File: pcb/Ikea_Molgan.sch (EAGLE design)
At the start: 21 parts, among them U2 MEGA328P-AU

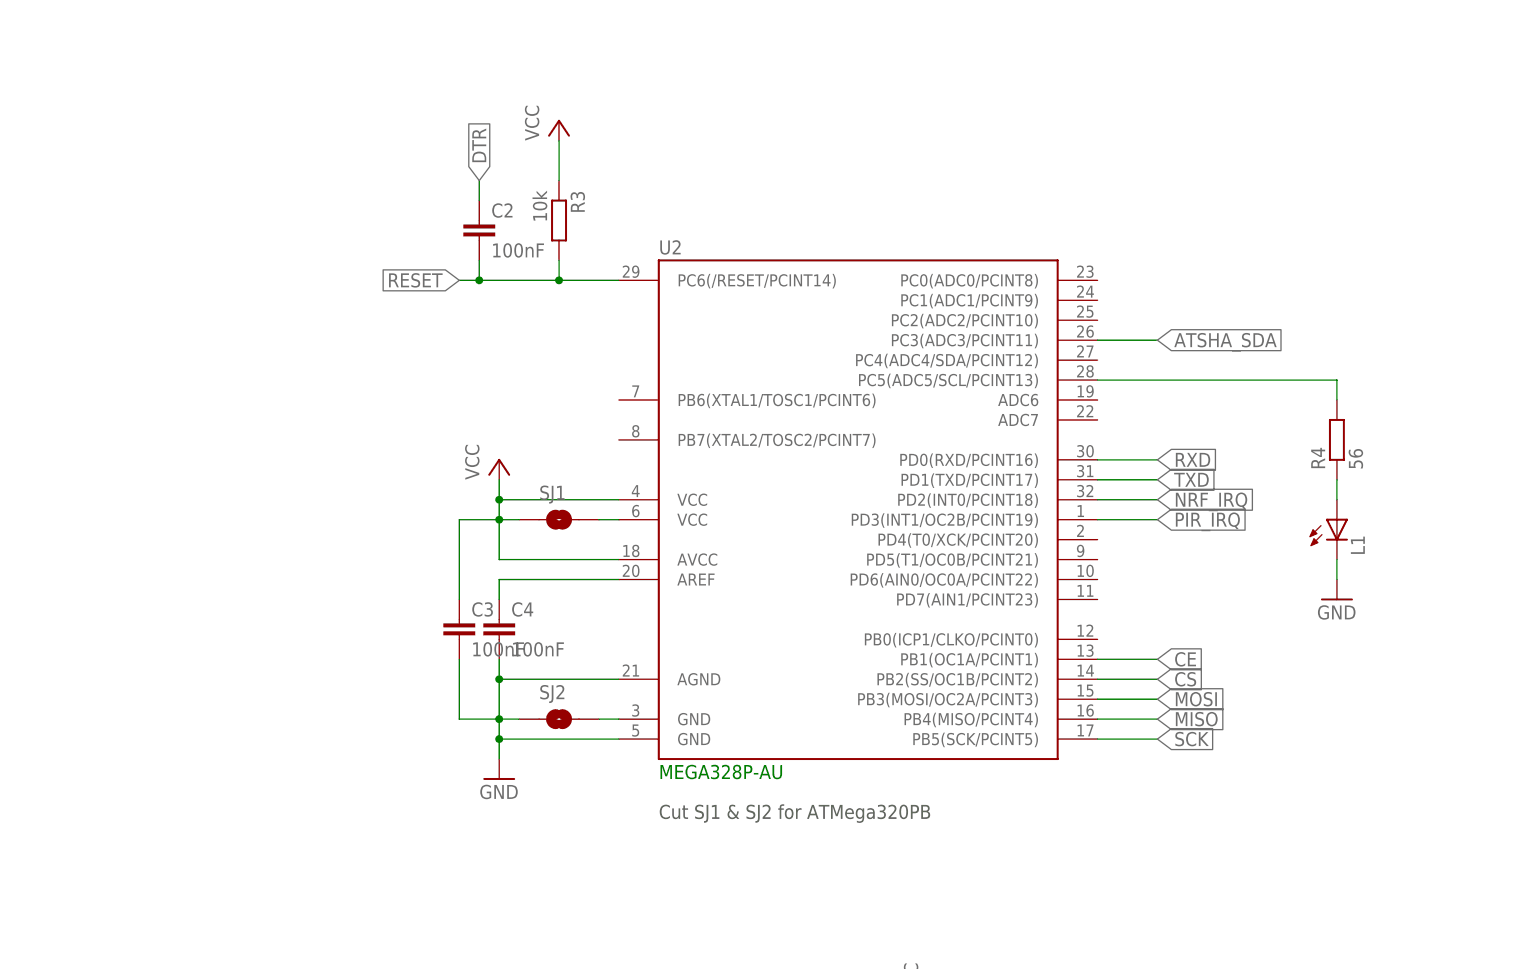
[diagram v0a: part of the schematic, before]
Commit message: Temperatursensor hinzugefügt und LED entfernt
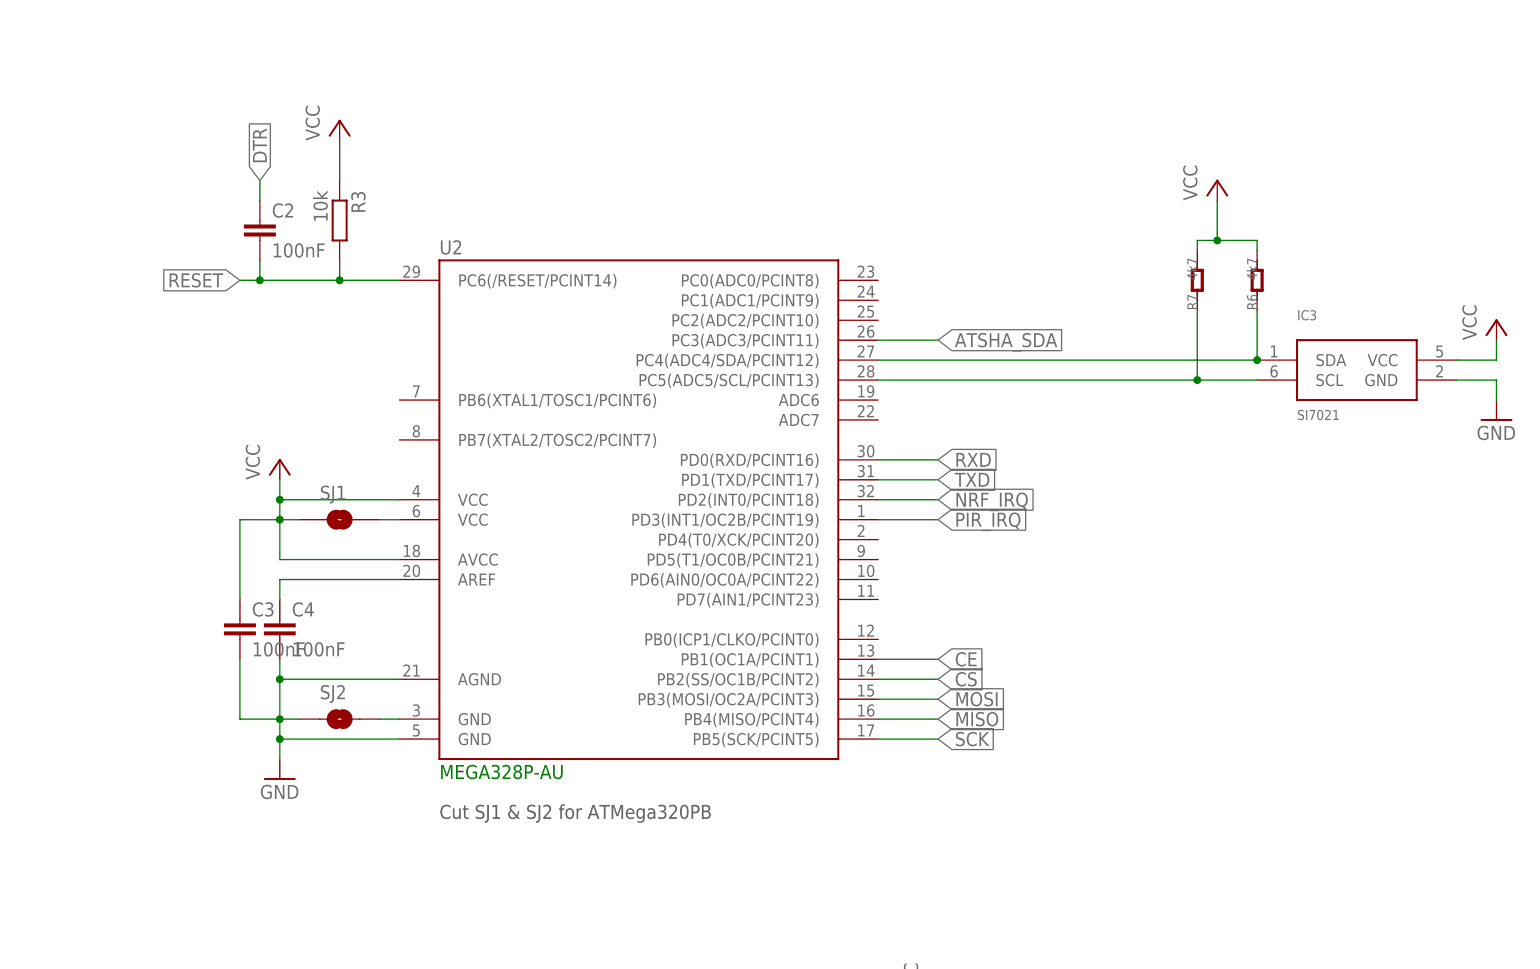
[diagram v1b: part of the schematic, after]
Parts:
- removed L1: (no value), adafruit:LEDCHIPLED_0805
- removed R4: 56, rcl:R-EU_R0805
- added IC3: SI7021, Sensor:SI7021
- added R6, R7: 4k7, Discrete:R-0402
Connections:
- removed net N$2: L1.A, R4.1
- removed net N$3: R4.2, U2.PC5(ADC5/SCL/PCINT13)
- new net SCL: IC3.SCL, R7.1, U2.PC5(ADC5/SCL/PCINT13)
- new net SDA: IC3.SDA, R6.1, U2.PC4(ADC4/SDA/PCINT12)
- net GND: now also IC3.GND; no longer L1.C
- net VCC: now also IC3.VCC, R6.2, R7.2
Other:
- moved on the sheet: C2, C3, C4, R3, SJ1, SJ2, U2
